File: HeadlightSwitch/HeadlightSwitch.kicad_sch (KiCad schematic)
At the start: 24 parts, among them J0 Battery-, J101 Battery+, J102 MarkerTail+, J103 Headlight+, J104 Headlight-, Q101 BCX56, SW101 SW_Rotary3x4, U101 LM555xM

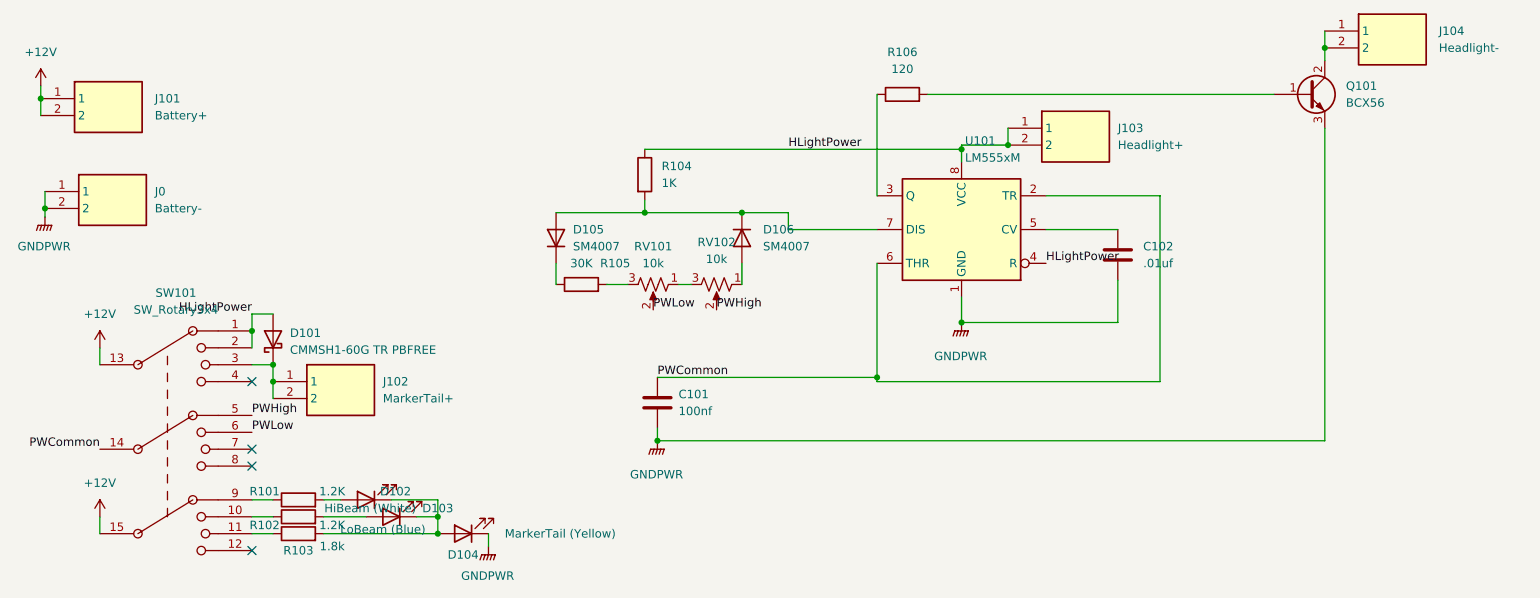
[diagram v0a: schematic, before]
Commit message: Complete Headlight Switch Board.
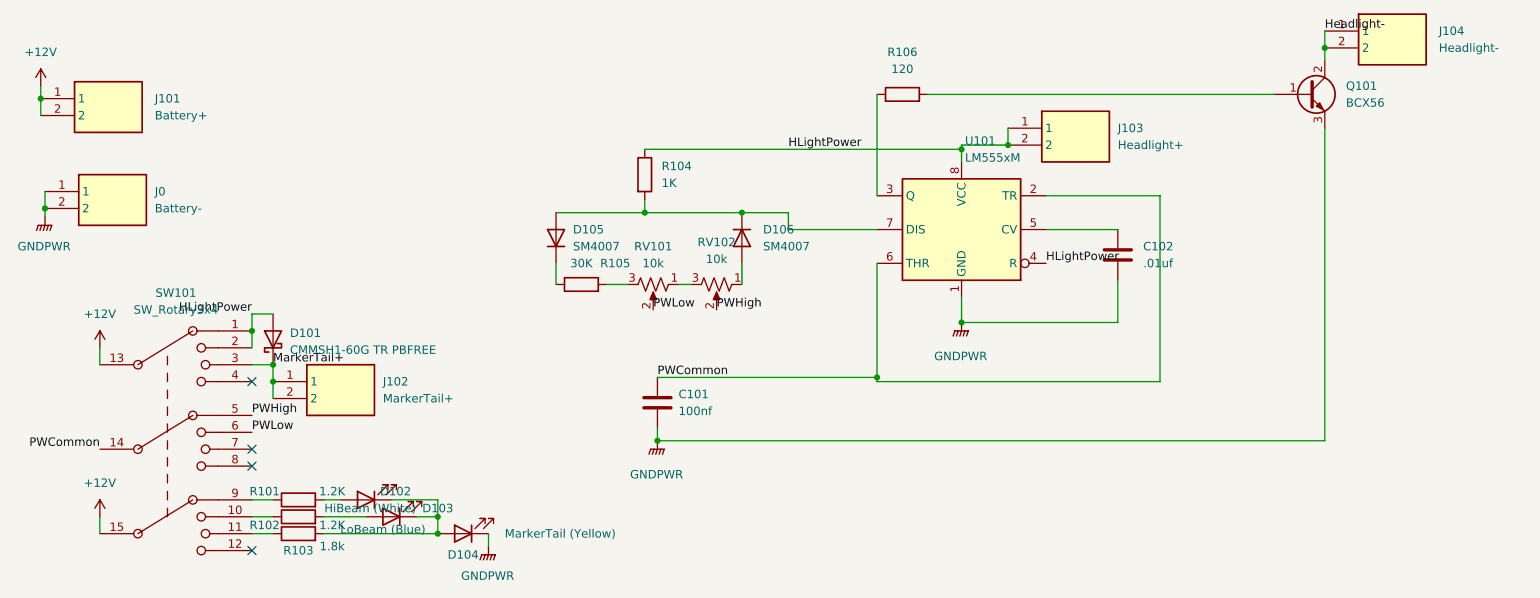
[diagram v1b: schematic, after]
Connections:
- net Headlight-: now reaches J104.1, J104.2, Q101.2 (C)
- net MarkerTail+: now reaches D101.1 (K), J102.1, J102.2, SW101.3
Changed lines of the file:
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@@
     (effects (font (size 1.27 1.27)) (justify right bottom))
+  )
+  (label "Headlight-" (at 231.775 28.575 0)
+    (effects (font (size 1.27 1.27)) (justify left bottom))
   )
   (label "PWHigh" (at 140.335 70.485 0)
@@
     (effects (font (size 1.27 1.27)) (justify right bottom))
   )
+  (label "MarkerTail+" (at 73.66 78.74 0)
+    (effects (font (size 1.27 1.27)) (justify left bottom))
+  )
   (symbol (lib_id "power:GNDPWR") (at 39.37 56.515 0) (unit 1)
